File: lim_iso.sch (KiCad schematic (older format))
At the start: 64 parts

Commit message: started pcb layout
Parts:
- removed R? (x2): 5K, Resistors_SMD:R_1206, symbol R
- gave numbers to parts that had none: 62
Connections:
- wire segments 127 -> 123

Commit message: added opto and DE footprints
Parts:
- removed R338, R339: 100K, Resistors_SMD:R_1206, symbol R
- removed U301, U302: 4N25, Opto-Devices:Optocoupler_SMD_ReflowWaveSoldering_KPC357_LTV35x_PC357_SingleChannel, symbol 4N25
- added U301, U302: TCMT1108, CNCbreakout:TCMT1108, symbol TLP291
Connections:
- wire segments 123 -> 115
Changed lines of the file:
@@
 LIBS:valves
 LIBS:references
+LIBS:FabLab
 LIBS:CNCbreakout-cache
 EELAYER 25 0
@@
 	1    0    0    -1
 $EndComp
-Connection ~ 8750 4800
-Wire Wire Line
-	9150 4600 9050 4600
-Wire Wire Line
-	9150 4800 9150 4600
-Wire Wire Line
-	8750 4800 8750 4900
-Text GLabel 8750 4900 2    60   Input ~ 0
+Text GLabel 8750 4800 2    60   Input ~ 0
 DGND
 Wire Wire Line
-	9150 5600 9050 5600
-Wire Wire Line
-	9150 5800 9150 5600
-Wire Wire Line
-	8650 4600 8750 4600
-Wire Wire Line
-	8650 5600 8750 5600
-$Comp
-L R R339
-U 1 1 5791DCE1
-P 8900 5600
-F 0 "R339" V 8980 5600 50  0000 C CNN
-F 1 "100K" V 8900 5600 50  0000 C CNN
-F 2 "Resistors_SMD:R_1206" V 8830 5600 50  0001 C CNN
-F 3 "" H 8900 5600 50  0000 C CNN
-	1    8900 5600
-	0    -1   -1   0
-$EndComp
-$Comp
-L R R338
-U 1 1 5791DCE0
-P 8900 4600
-F 0 "R338" V 8980 4600 50  0000 C CNN
-F 1 "100K" V 8900 4600 50  0000 C CNN
-F 2 "Resistors_SMD:R_1206" V 8830 4600 50  0001 C CNN
-F 3 "" H 8900 4600 50  0000 C CNN
-	1    8900 4600
-	0    -1   -1   0
-$EndComp
-Wire Wire Line
-	8750 4700 8650 4700
-Wire Wire Line
-	8750 5700 8650 5700
-Connection ~ 8750 5800
-Wire Wire Line
-	8650 4800 9150 4800
-Wire Wire Line
-	8750 5800 8750 5900
-Wire Wire Line
-	8650 5800 9150 5800
-Text GLabel 8750 5900 2    60   Input ~ 0
+	8750 4600 8650 4600
+Wire Wire Line
+	8750 5600 8650 5600
+Text GLabel 8750 5800 2    60   Input ~ 0
 DGND
-$Comp
-L 4N25 U302
-U 1 1 5791DCDD
-P 8350 5700
-F 0 "U302" H 8150 5900 50  0000 L CNN
-F 1 "4N25" H 8350 5900 50  0000 L CNN
-F 2 "Opto-Devices:Optocoupler_SMD_ReflowWaveSoldering_KPC357_LTV35x_PC357_SingleChannel" H 8150 5500 50  0000 L CIN
-F 3 "" H 8350 5700 50  0000 L CNN
-	1    8350 5700
-	1    0    0    -1
-$EndComp
-$Comp
-L 4N25 U301
-U 1 1 5791DCDC
-P 8350 4700
-F 0 "U301" H 8150 4900 50  0000 L CNN
-F 1 "4N25" H 8350 4900 50  0000 L CNN
-F 2 "Opto-Devices:Optocoupler_SMD_ReflowWaveSoldering_KPC357_LTV35x_PC357_SingleChannel" H 8150 4500 50  0000 L CIN
-F 3 "" H 8350 4700 50  0000 L CNN
-	1    8350 4700
-	1    0    0    -1
-$EndComp
-Text GLabel 8750 5700 2    60   Input ~ 0
+Text GLabel 8750 5600 2    60   Input ~ 0
 DOut_2
-Text GLabel 8750 4700 2    60   Input ~ 0
+Text GLabel 8750 4600 2    60   Input ~ 0
 DOut_1
 Connection ~ 8500 1300
@@
 Wire Wire Line
 	5600 1600 6200 1600
+$Comp
+L TLP291 U302
+U 1 1 57BAE046
+P 8350 5700
+F 0 "U302" H 8150 5900 50  0000 L CNN
+F 1 "TCMT1108" H 8350 5900 50  0000 L CNN
+F 2 "CNCbreakout:TCMT1108" H 8150 5500 50  0000 L CIN
+F 3 "" H 8350 5700 50  0000 L CNN
+	1    8350 5700
+	1    0    0    -1
+$EndComp
+$Comp
+L TLP291 U301
+U 1 1 57BAE949
+P 8350 4700
+F 0 "U301" H 8150 4900 50  0000 L CNN
+F 1 "TCMT1108" H 8350 4900 50  0000 L CNN
+F 2 "CNCbreakout:TCMT1108" H 8150 4500 50  0000 L CIN
+F 3 "" H 8350 4700 50  0000 L CNN
+	1    8350 4700
+	1    0    0    -1
+$EndComp
+Wire Wire Line
+	8750 4800 8650 4800
+Wire Wire Line
+	8650 5800 8750 5800
 $EndSCHEMATC

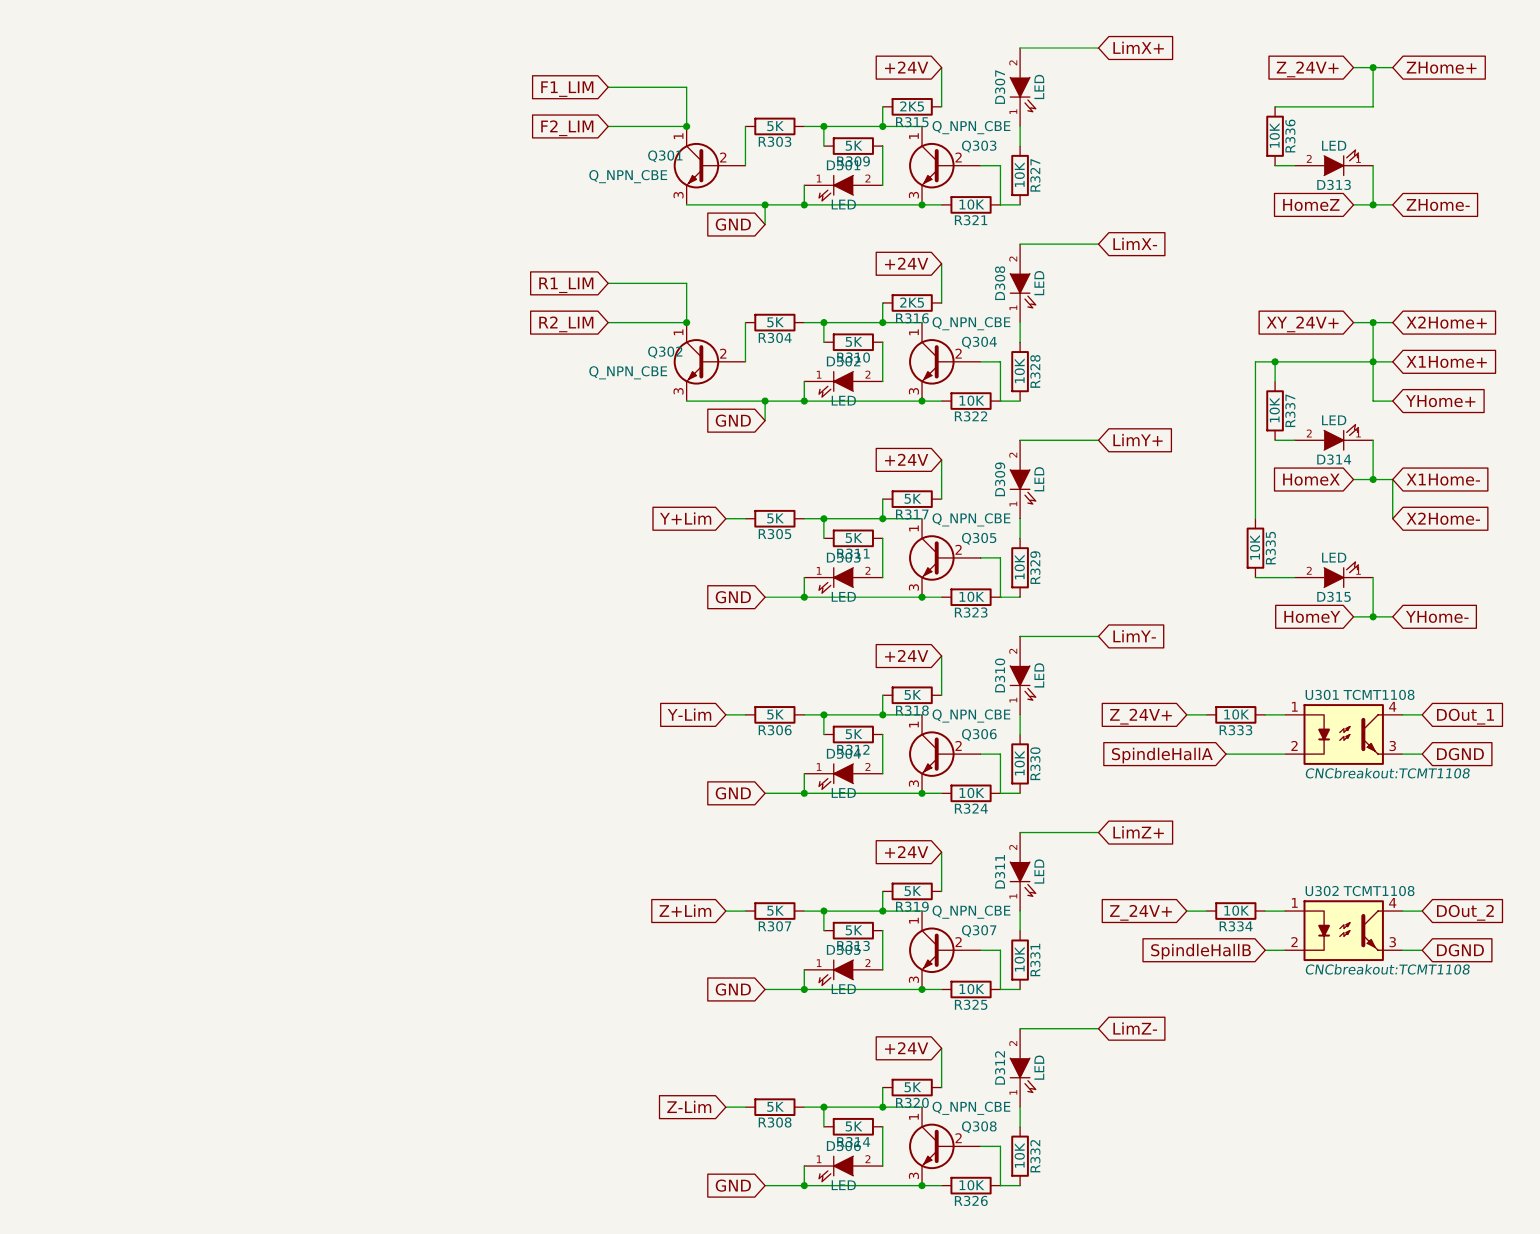
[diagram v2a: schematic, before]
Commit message: set limits to pull down, optional invert
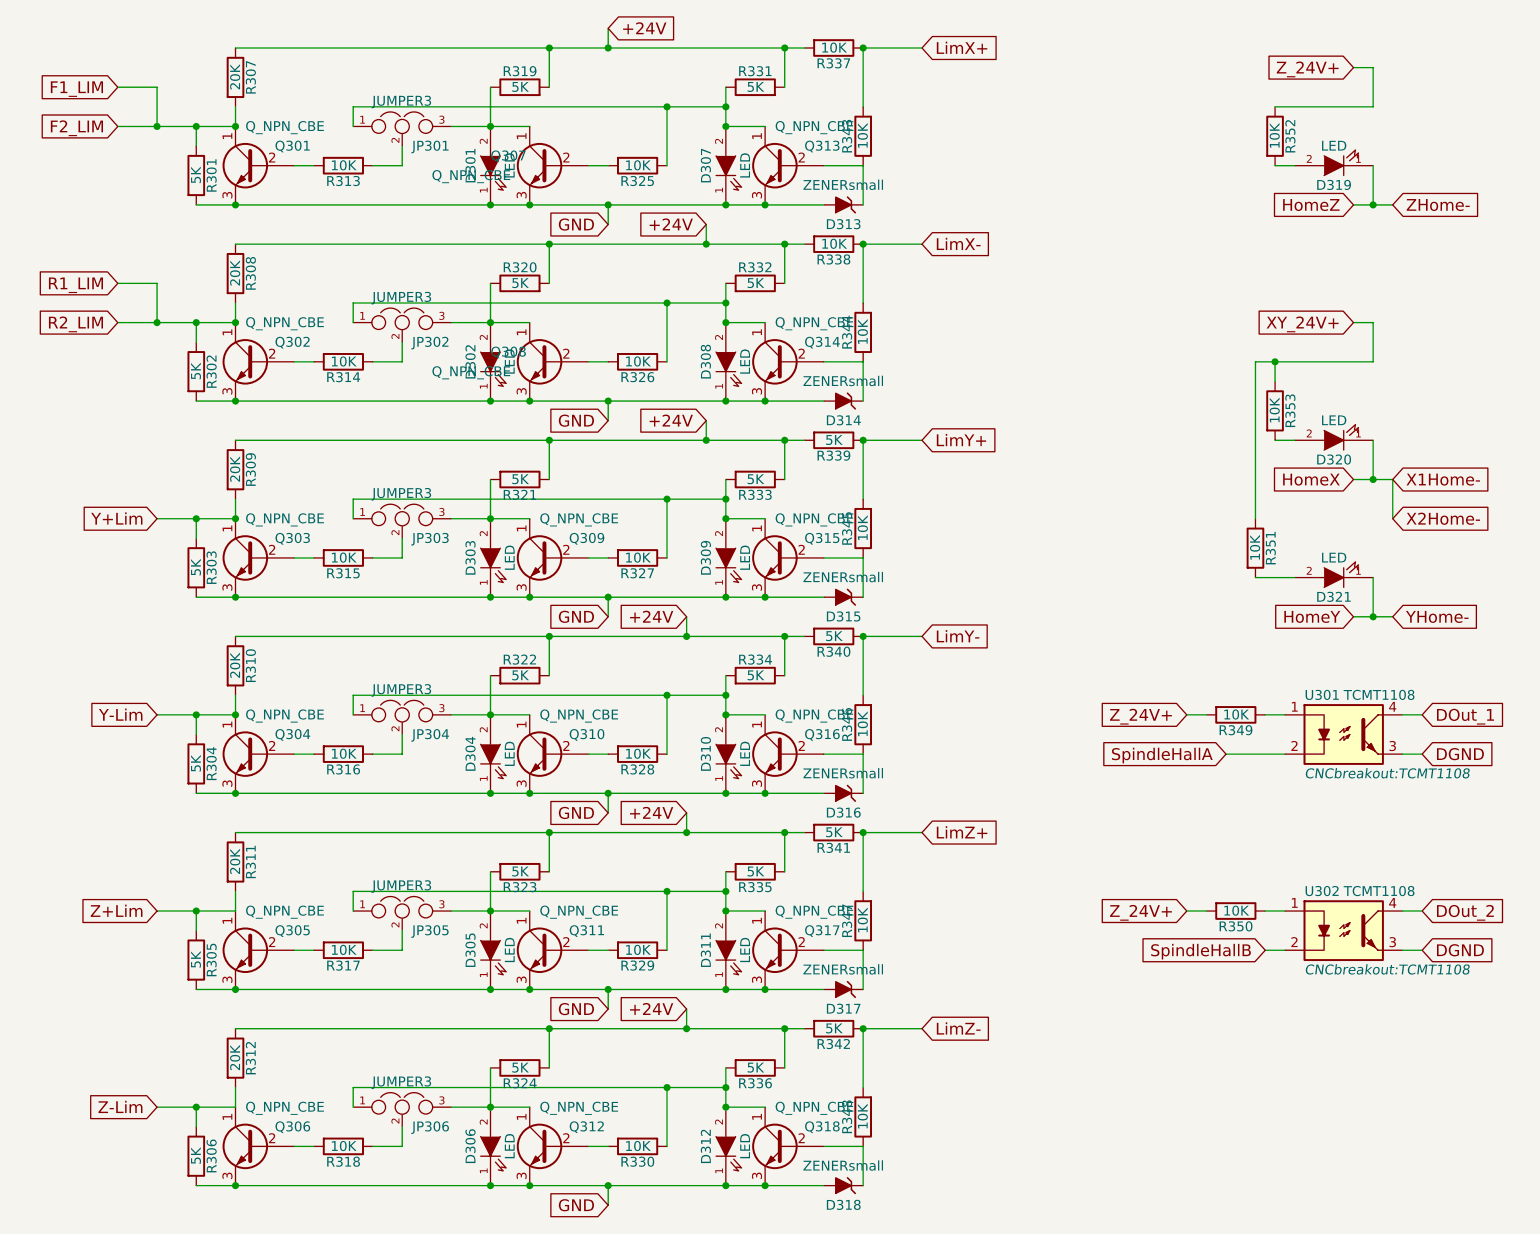
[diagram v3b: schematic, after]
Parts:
- added D313, D314, D315, D316, D317, D318: ZENERsmall, Diodes_SMD:SOD-123, symbol ZENERsmall
- added JP301, JP302, JP303, JP304, JP305, JP306: JUMPER3, CNCbreakout:JumperDouble, symbol JUMPER3
- added Q301, Q302, Q303, Q304, Q305, Q306, Q309, Q310, Q311, Q312: Q_NPN_CBE, TO_SOT_Packages_SMD:SOT-23, symbol Q_NPN_CBE
- added R301, R302, R303, R304, R305, R306: 5K, Resistors_SMD:R_1206, symbol R
- added R307, R308, R309, R310, R311, R312: 20K, Resistors_SMD:R_1206, symbol R
- added R343, R344, R345, R346, R347, R348: 10K, Resistors_SMD:R_1206, symbol R
- R337: renamed from R315; value 2K5 -> 10K
- R338: renamed from R316; value 2K5 -> 10K
- renumbered D307 to D301, D308 to D302, D309 to D303, D310 to D304, D311 to D305, D312 to D306, D301 to D307, D302 to D308, D303 to D309, D304 to D310, D305 to D311, D306 to D312, D313 to D319, D314 to D320, D315 to D321, Q301 to Q307, Q302 to Q308, Q303 to Q313, Q304 to Q314, Q305 to Q315, Q306 to Q316, Q307 to Q317, Q308 to Q318, R321 to R313, R322 to R314, R323 to R315, R324 to R316, R325 to R317, R326 to R318, R303 to R319, R304 to R320, R305 to R321, R306 to R322, R307 to R323, R308 to R324, R327 to R325, R328 to R326, R329 to R327, R330 to R328, R331 to R329, R332 to R330, R309 to R331, R310 to R332, R311 to R333, R312 to R334, R313 to R335, R314 to R336, R317 to R339, R318 to R340, R319 to R341, R320 to R342, R333 to R349, R334 to R350, R335 to R351, R336 to R352, R337 to R353
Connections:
- net +24V: now also R319.2, R320.2, R321.1, R322.1, R323.1, R324.1, R331.2, R332.1, R333.1, R334.1, R335.1, R336.1, R337.2, R338.2, R339.2, R340.2, R341.2, R342.2, R307.1, R308.1, R309.1, R310.1, R311.1, R312.1; no longer R337.1, R338.1, R339.1, R340.1, R341.1, R342.1
- net F1_LIM: now also Q301.1 (C), R301.1, R307.2; no longer Q307.1 (C)
- net GND: now also D301.1 (K), D302.1 (K), D303.1 (K), D304.1 (K), D305.1 (K), D306.1 (K), D313.2 (A), D314.2 (A), D315.2 (A), D316.2 (A), D317.2 (A), D318.2 (A), Q301.3 (E), Q302.3 (E), Q303.3 (E), Q304.3 (E), Q305.3 (E), Q306.3 (E), Q309.3 (E), Q310.3 (E), Q311.3 (E), Q312.3 (E), R301.2, R302.2, R303.2, R304.2, R305.2, R306.2; no longer R313.2, R314.2, R315.2, R316.2, R317.2, R318.2
- net LimX+: now also R337.1, R343.2; no longer D301.2 (A)
- net LimX-: now also R338.1, R344.2; no longer D302.2 (A)
- net LimY+: now also R339.1, R345.2; no longer D303.2 (A)
- net LimY-: now also R340.1, R346.2; no longer D304.2 (A)
- net LimZ+: now also R341.1, R347.2; no longer D305.2 (A)
- net LimZ-: now also R342.1, R348.2; no longer D306.2 (A)
- net R1_LIM: now also Q302.1 (C), R302.1, R308.2; no longer Q308.1 (C)
- net Y+Lim: now also Q303.1 (C), R303.1, R309.2; no longer R321.2
- net Y-Lim: now also Q304.1 (C), R304.1, R310.2; no longer R322.2
- net Z+Lim: now also Q305.1 (C), R305.1, R311.2; no longer R323.2
- net Z-Lim: now also Q306.1 (C), R306.1, R312.2; no longer R324.2
- net at Q307.2 (B): now also R325.2; no longer R319.2
- net at R325.1: now also D307.2 (A), Q313.1 (C), R331.1, JP301.1; no longer D301.1 (K)
- net at Q308.2 (B): now also R326.2; no longer R320.2
- net at Q314.1 (C), R332.2: now also D308.2 (A), R326.1, JP302.1; no longer R320.1, R338.2
- net at Q315.1 (C), R333.2: now also D309.2 (A), R327.1, JP303.1; no longer R321.1, R339.2
- net at Q316.1 (C), R334.2: now also D310.2 (A), R328.1, JP304.1; no longer R322.1, R340.2
- net at Q317.1 (C), R335.2: now also D311.2 (A), R329.1, JP305.1; no longer R323.1, R341.2
- net at Q318.1 (C), R336.2: now also D312.2 (A), R330.1, JP306.1; no longer R324.1, R342.2
- net X1Home+ renamed XY_24V+
- net ZHome+ renamed Z_24V+
- new net: D301.2 (A), JP301.3, Q307.1 (C), R319.1
- new net: D313.1 (K), Q313.2 (B), R343.1
- new net: JP301.2, R313.1
- new net: Q301.2 (B), R313.2
- new net: D302.2 (A), JP302.3, Q308.1 (C), R320.1
- new net: D314.1 (K), Q314.2 (B), R344.1
- new net: JP302.2, R314.1
- new net: Q302.2 (B), R314.2
- new net: Q309.2 (B), R327.2
- new net: D315.1 (K), Q315.2 (B), R345.1
- new net: JP303.2, R315.1
- new net: Q303.2 (B), R315.2
- new net: D303.2 (A), JP303.3, Q309.1 (C), R321.2
- new net: Q310.2 (B), R328.2
- new net: D316.1 (K), Q316.2 (B), R346.1
- new net: JP304.2, R316.1
- new net: Q304.2 (B), R316.2
- new net: D304.2 (A), JP304.3, Q310.1 (C), R322.2
- new net: Q311.2 (B), R329.2
- new net: D317.1 (K), Q317.2 (B), R347.1
- new net: JP305.2, R317.1
- new net: Q305.2 (B), R317.2
- new net: D305.2 (A), JP305.3, Q311.1 (C), R323.2
- new net: Q312.2 (B), R330.2
- new net: D318.1 (K), Q318.2 (B), R348.1
- new net: JP306.2, R318.1
- new net: Q306.2 (B), R318.2
- new net: D306.2 (A), JP306.3, Q312.1 (C), R324.2
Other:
- moved on the sheet: D301, D302, D303, D304, D305, D306, D307, D308, D309, D310, D311, D312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
